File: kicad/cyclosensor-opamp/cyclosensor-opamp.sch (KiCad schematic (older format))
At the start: 11 parts, among them J1 RJ14, U1 LM358, U2 TCRT5000

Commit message: various changes to schematics
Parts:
- removed RV1, RV2: POT, ~, symbol POT
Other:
- moved on the sheet: GAIN1, J1, OFFSET1, R1, R2, R3, R5, U1A, U2

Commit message: updating basic cyclo-sensor.  Still need to verify with actual cyclophone.
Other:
- note added: "1M ok for tuning, not too sensitive?"
- note added: "Ok to have 5V without 'pair' here?"
- note added: "offset from which side? zero or 5v/1024?"
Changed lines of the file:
@@
 Sheet 1 1
 Title ""
-Date "5 apr 2014"
+Date "6 apr 2014"
 Rev ""
 Comp ""
@@
 Wire Wire Line
 	6800 3800 6800 3500
+Text Notes 6200 4200 0    60   ~ 0
+Ok to have 5V without 'pair' here?
+Text Notes 3200 5550 0    60   ~ 0
+offset from which side?  zero or 5v/1024?
+Text Notes 4100 3150 0    60   ~ 0
+1M ok for tuning, not too sensitive?
 $EndSCHEMATC

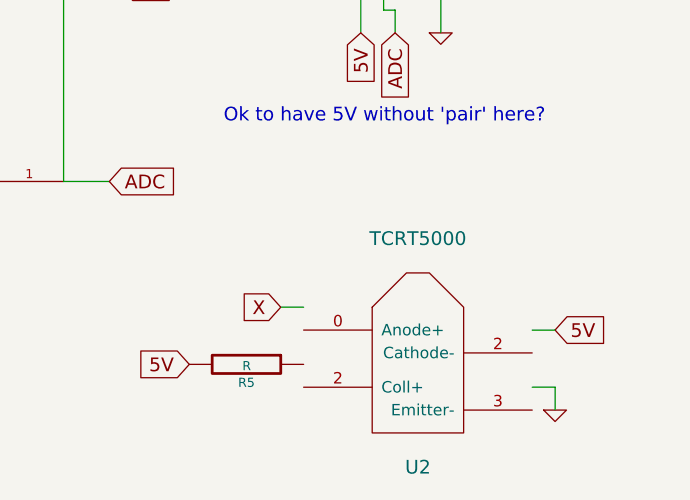
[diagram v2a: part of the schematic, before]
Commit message: add two voltage regulation circuits, the TL431 and LM317 based.  Also update some things - REFP is 2.5v, while AREF is 5v
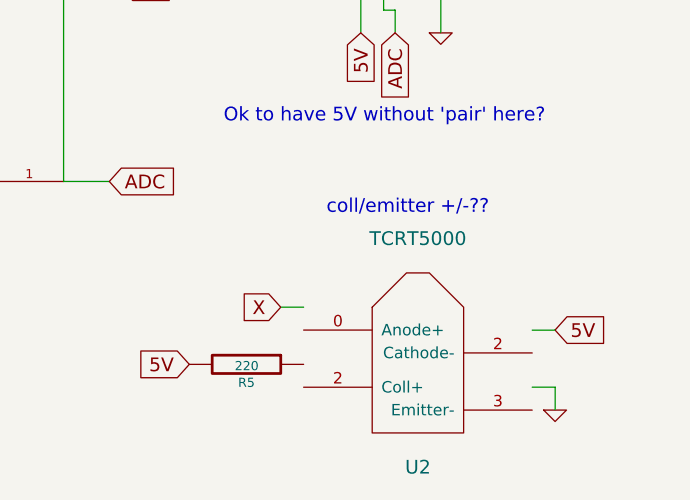
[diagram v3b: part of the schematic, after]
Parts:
- R5: value R -> 220
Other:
- note added: "coll/emitter +/-??"
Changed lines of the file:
@@
 P 6300 5250
 F 0 "R5" V 6380 5250 40  0000 C CNN
-F 1 "R" V 6307 5251 40  0000 C CNN
+F 1 "220" V 6307 5251 40  0000 C CNN
 F 2 "~" V 6230 5250 30  0000 C CNN
 F 3 "~" H 6300 5250 30  0000 C CNN
@@
 Text Notes 4100 3150 0    60   ~ 0
 1M ok for tuning, not too sensitive?
+Text Notes 6650 4600 0    60   ~ 0
+coll/emitter +/-??
 $EndSCHEMATC

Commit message: various changes!  notes frm Dan.
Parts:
- added C?: .01uf, ~, symbol C
- added C?: 10uf, ~, symbol C
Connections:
- wire segments 29 -> 33
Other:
- note added: "Ok to have 5V without 'pair' here? \nYES"
- note added: "Put near pin 8 on op-amp!"
- note added: "option of two caps \nfor different freq\nfiltering on each"
- note removed: "Ok to have 5V without 'pair' here?"
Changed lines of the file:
@@
 Sheet 1 1
 Title ""
-Date "6 apr 2014"
+Date "9 apr 2014"
 Rev ""
 Comp ""
@@
 	6800 3800 6800 3500
 Text Notes 6200 4200 0    60   ~ 0
-Ok to have 5V without 'pair' here?
+Ok to have 5V without 'pair' here?  \nYES
 Text Notes 3200 5550 0    60   ~ 0
 offset from which side?  zero or 5v/1024?
 Text Notes 4100 3150 0    60   ~ 0
 1M ok for tuning, not too sensitive?
-Text Notes 6650 4600 0    60   ~ 0
+Text Notes 6600 5950 0    60   ~ 0
 coll/emitter +/-??
+$Comp
+L C C?
+U 1 1 53449FBF
+P 8050 3800
+F 0 "C?" H 8050 3900 40  0000 L CNN
+F 1 ".01uf" H 8056 3715 40  0000 L CNN
+F 2 "~" H 8088 3650 30  0000 C CNN
+F 3 "~" H 8050 3800 60  0000 C CNN
+	1    8050 3800
+	1    0    0    -1
+$EndComp
+Text GLabel 8050 3450 1    60   Input ~ 0
+5V
+$Comp
+L GND #PWR?
+U 1 1 53449FDD
+P 8050 4100
+F 0 "#PWR?" H 8050 4100 30  0001 C CNN
+F 1 "GND" H 8050 4030 30  0001 C CNN
+F 2 "" H 8050 4100 60  0000 C CNN
+F 3 "" H 8050 4100 60  0000 C CNN
+	1    8050 4100
+	1    0    0    -1
+$EndComp
+Wire Wire Line
+	8050 4000 8050 4100
+Wire Wire Line
+	8050 3450 8050 3600
+Text Notes 7800 3200 0    60   ~ 0
+Put near pin 8 on op-amp!
+$Comp
+L C C?
+U 1 1 5344A0AE
+P 8400 3800
+F 0 "C?" H 8400 3900 40  0000 L CNN
+F 1 "10uf" H 8406 3715 40  0000 L CNN
+F 2 "~" H 8438 3650 30  0000 C CNN
+F 3 "~" H 8400 3800 60  0000 C CNN
+	1    8400 3800
+	1    0    0    -1
+$EndComp
+Text GLabel 8400 3450 1    60   Input ~ 0
+5V
+$Comp
+L GND #PWR?
+U 1 1 5344A0B5
+P 8400 4100
+F 0 "#PWR?" H 8400 4100 30  0001 C CNN
+F 1 "GND" H 8400 4030 30  0001 C CNN
+F 2 "" H 8400 4100 60  0000 C CNN
+F 3 "" H 8400 4100 60  0000 C CNN
+	1    8400 4100
+	1    0    0    -1
+$EndComp
+Wire Wire Line
+	8400 4000 8400 4100
+Wire Wire Line
+	8400 3450 8400 3600
+Text Notes 8050 4350 0    60   ~ 0
+option of two caps \nfor different freq\nfiltering on each
 $EndSCHEMATC

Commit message: update tcrt5000
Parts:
- removed R3: 1K, ~, symbol R
- removed U2: TCRT5000, ~, symbol TCRT5000
- added OFFSET?: 20K, ~, symbol POT
- added R?: 20k, ~, symbol R
- added U?: TCRT5000, ~, symbol TCRT5000
- GAIN1: value 1M -> 100k
- R1, R2: value 1K -> 20k
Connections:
- wire segments 33 -> 36
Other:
- moved on the sheet: OFFSET1, R5
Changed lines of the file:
@@
 Sheet 1 1
 Title ""
-Date "9 apr 2014"
+Date "12 apr 2014"
 Rev ""
 Comp ""
@@
 	1    0    0    -1
 $EndComp
-$Comp
-L TCRT5000 U2
-U 1 1 532FB873
-P 7050 5150
-F 0 "U2" H 7050 4600 60  0000 C CNN
-F 1 "TCRT5000" H 7050 5600 60  0000 C CNN
-F 2 "~" H 7050 5150 60  0000 C CNN
-F 3 "~" H 7050 5150 60  0000 C CNN
-	1    7050 5150
-	1    0    0    -1
-$EndComp
 Text GLabel 6800 3800 3    60   Input ~ 0
 5V
@@
 	1    0    0    -1
 $EndComp
-Text GLabel 4900 3950 1    60   Input ~ 0
+Text GLabel 4900 4950 3    60   Input ~ 0
 5V
 $Comp
 L GND #PWR02
 U 1 1 533B8353
-P 4900 4950
-F 0 "#PWR02" H 4900 4950 30  0001 C CNN
-F 1 "GND" H 4900 4880 30  0001 C CNN
-F 2 "" H 4900 4950 60  0000 C CNN
-F 3 "" H 4900 4950 60  0000 C CNN
-	1    4900 4950
-	1    0    0    -1
+P 4900 3950
+F 0 "#PWR02" H 4900 3950 30  0001 C CNN
+F 1 "GND" H 4900 3880 30  0001 C CNN
+F 2 "" H 4900 3950 60  0000 C CNN
+F 3 "" H 4900 3950 60  0000 C CNN
+	1    4900 3950
+	-1   0    0    1
 $EndComp
 $Comp
@@
 F 3 "" H 5000 4450 60  0000 C CNN
 	1    5000 4450
-	1    0    0    -1
+	1    0    0    1
 $EndComp
 $Comp
@@
 P 4000 4350
 F 0 "R2" V 4080 4350 40  0000 C CNN
-F 1 "1K" V 4007 4351 40  0000 C CNN
+F 1 "20k" V 4007 4351 40  0000 C CNN
 F 2 "~" V 3930 4350 30  0000 C CNN
 F 3 "~" H 4000 4350 30  0000 C CNN
@@
 ADC
 $Comp
-L R R3
-U 1 1 533B9B66
-P 4400 4900
-F 0 "R3" V 4480 4900 40  0000 C CNN
-F 1 "1K" V 4407 4901 40  0000 C CNN
-F 2 "~" V 4330 4900 30  0000 C CNN
-F 3 "~" H 4400 4900 30  0000 C CNN
-	1    4400 4900
-	1    0    0    -1
-$EndComp
-$Comp
 L R R1
 U 1 1 533B9B87
 P 3650 4750
 F 0 "R1" V 3730 4750 40  0000 C CNN
-F 1 "1K" V 3657 4751 40  0000 C CNN
+F 1 "20k" V 3657 4751 40  0000 C CNN
 F 2 "~" V 3580 4750 30  0000 C CNN
 F 3 "~" H 3650 4750 30  0000 C CNN
@@
 	1    0    0    -1
 $EndComp
-Text GLabel 5750 3600 2    60   Input ~ 0
-5V
-Text GLabel 7650 5100 2    60   Input ~ 0
-5V
-$Comp
-L GND #PWR03
-U 1 1 533B9C11
-P 3650 5150
-F 0 "#PWR03" H 3650 5150 30  0001 C CNN
-F 1 "GND" H 3650 5080 30  0001 C CNN
-F 2 "" H 3650 5150 60  0000 C CNN
-F 3 "" H 3650 5150 60  0000 C CNN
-	1    3650 5150
-	1    0    0    -1
-$EndComp
-$Comp
-L GND #PWR04
-U 1 1 533B9C20
-P 4400 5300
-F 0 "#PWR04" H 4400 5300 30  0001 C CNN
-F 1 "GND" H 4400 5230 30  0001 C CNN
-F 2 "" H 4400 5300 60  0000 C CNN
-F 3 "" H 4400 5300 60  0000 C CNN
-	1    4400 5300
-	1    0    0    -1
-$EndComp
-Text GLabel 6450 5000 0    60   Input ~ 0
+Text GLabel 2750 3750 0    60   Input ~ 0
 X
 Text GLabel 3550 4350 0    60   Input ~ 0
 X
-Text GLabel 6050 5250 0    60   Input ~ 0
+Text GLabel 2350 3500 0    60   Input ~ 0
 5V
 $Comp
 L GND #PWR05
 U 1 1 533B9F2F
-P 7650 5450
-F 0 "#PWR05" H 7650 5450 30  0001 C CNN
-F 1 "GND" H 7650 5380 30  0001 C CNN
-F 2 "" H 7650 5450 60  0000 C CNN
-F 3 "" H 7650 5450 60  0000 C CNN
-	1    7650 5450
+P 3950 3950
+F 0 "#PWR05" H 3950 3950 30  0001 C CNN
+F 1 "GND" H 3950 3880 30  0001 C CNN
+F 2 "" H 3950 3950 60  0000 C CNN
+F 3 "" H 3950 3950 60  0000 C CNN
+	1    3950 3950
 	1    0    0    -1
 $EndComp
@@
 L R R5
 U 1 1 533B9FB6
-P 6300 5250
-F 0 "R5" V 6380 5250 40  0000 C CNN
-F 1 "220" V 6307 5251 40  0000 C CNN
-F 2 "~" V 6230 5250 30  0000 C CNN
-F 3 "~" H 6300 5250 30  0000 C CNN
-	1    6300 5250
+P 2600 3500
+F 0 "R5" V 2680 3500 40  0000 C CNN
+F 1 "220" V 2607 3501 40  0000 C CNN
+F 2 "~" V 2530 3500 30  0000 C CNN
+F 3 "~" H 2600 3500 30  0000 C CNN
+	1    2600 3500
 	0    1    1    0
 $EndComp
 NoConn ~ 6700 3500
 NoConn ~ 7200 3500
-Wire Wire Line
-	7000 3500 7000 3650
-Wire Wire Line
-	7000 3650 7150 3650
-Wire Wire Line
-	4500 3450 4500 4350
-Wire Wire Line
-	4500 4350 4250 4350
-Wire Wire Line
-	3550 4350 3750 4350
-Wire Wire Line
-	3650 4350 3650 4500
-Connection ~ 3650 4350
-Wire Wire Line
-	6450 5000 6550 5000
-Wire Wire Line
-	7650 5100 7550 5100
-Wire Wire Line
-	5500 4450 5700 4450
-Wire Wire Line
-	4050 4550 4500 4550
-Wire Wire Line
-	4400 4550 4400 4650
-Wire Wire Line
-	4400 5150 4400 5300
-Wire Wire Line
-	3650 5000 3650 5150
-Wire Wire Line
-	5500 4450 5500 3600
-Connection ~ 5500 3600
-Wire Wire Line
-	4900 3950 4900 4050
-Wire Wire Line
-	6900 3500 6900 3700
-Wire Wire Line
-	6900 3700 6950 3700
-Wire Wire Line
-	6950 3700 6950 3800
-Wire Wire Line
-	7550 5350 7650 5350
-Wire Wire Line
-	7650 5350 7650 5450
 $Comp
 L POT GAIN1
@@
 P 4900 3450
 F 0 "GAIN1" H 4900 3350 50  0000 C CNN
-F 1 "1M" H 4900 3450 50  0000 C CNN
+F 1 "100k" H 4900 3450 50  0000 C CNN
 F 2 "~" H 4900 3450 60  0000 C CNN
 F 3 "~" H 4900 3450 60  0000 C CNN
@@
 	1    0    0    -1
 $EndComp
-Wire Wire Line
-	4500 3450 4650 3450
-Wire Wire Line
-	4900 3300 5250 3300
-Wire Wire Line
-	5250 3300 5250 3600
-Connection ~ 5250 3600
 NoConn ~ 5150 3450
-Wire Wire Line
-	5250 3600 5750 3600
 $Comp
 L POT OFFSET1
 U 1 1 533BA12C
-P 4050 4900
-F 0 "OFFSET1" H 4050 4800 50  0000 C CNN
-F 1 "20K" H 4050 4900 50  0000 C CNN
-F 2 "~" H 4050 4900 60  0000 C CNN
-F 3 "~" H 4050 4900 60  0000 C CNN
-	1    4050 4900
+P 4200 4800
+F 0 "OFFSET1" H 4200 4700 50  0000 C CNN
+F 1 "20K" H 4200 4800 50  0000 C CNN
+F 2 "~" H 4200 4800 60  0000 C CNN
+F 3 "~" H 4200 4800 60  0000 C CNN
+	1    4200 4800
 	0    1    1    0
 $EndComp
-Wire Wire Line
-	4050 4550 4050 4650
-Connection ~ 4400 4550
-Text GLabel 4200 5200 3    60   Input ~ 0
-5V
-Wire Wire Line
-	4200 4900 4200 5200
-NoConn ~ 4050 5150
-Wire Wire Line
-	4900 4850 4900 4950
-Wire Wire Line
-	7150 3650 7150 3800
+Text GLabel 4050 4550 0    60   Input ~ 0
+5V
 NoConn ~ 7100 3500
-Wire Wire Line
-	6800 3800 6800 3500
 Text Notes 6200 4200 0    60   ~ 0
 Ok to have 5V without 'pair' here?  \nYES
@@
 	1    0    0    -1
 $EndComp
-Wire Wire Line
-	8050 4000 8050 4100
-Wire Wire Line
-	8050 3450 8050 3600
 Text Notes 7800 3200 0    60   ~ 0
 Put near pin 8 on op-amp!
@@
 	1    0    0    -1
 $EndComp
-Wire Wire Line
-	8400 4000 8400 4100
-Wire Wire Line
-	8400 3450 8400 3600
 Text Notes 8050 4350 0    60   ~ 0
 option of two caps \nfor different freq\nfiltering on each
+$Comp
+L TCRT5000 U?
+U 1 1 53499E1E
+P 3350 3550
+F 0 "U?" H 3350 3000 60  0000 C CNN
+F 1 "TCRT5000" H 3350 4000 60  0000 C CNN
+F 2 "~" H 3350 3550 60  0000 C CNN
+F 3 "~" H 3350 3550 60  0000 C CNN
+	1    3350 3550
+	1    0    0    -1
+$EndComp
+Wire Wire Line
+	7000 3500 7000 3650
+Wire Wire Line
+	7000 3650 7150 3650
+Wire Wire Line
+	4500 3450 4500 4350
+Wire Wire Line
+	4500 4350 4250 4350
+Wire Wire Line
+	3550 4350 3750 4350
+Wire Wire Line
+	3650 4350 3650 4500
+Connection ~ 3650 4350
+Wire Wire Line
+	2750 3750 2850 3750
+Wire Wire Line
+	5500 4450 5700 4450
+Wire Wire Line
+	3650 5000 3650 5150
+Wire Wire Line
+	4900 3950 4900 4050
+Wire Wire Line
+	6900 3500 6900 3700
+Wire Wire Line
+	6900 3700 6950 3700
+Wire Wire Line
+	6950 3700 6950 3800
+Wire Wire Line
+	3850 3850 3950 3850
+Wire Wire Line
+	3950 3600 3950 3950
+Wire Wire Line
+	4500 3450 4650 3450
+Wire Wire Line
+	4900 4850 4900 4950
+Wire Wire Line
+	7150 3650 7150 3800
+Wire Wire Line
+	6800 3800 6800 3500
+Wire Wire Line
+	8050 4000 8050 4100
+Wire Wire Line
+	8050 3450 8050 3600
+Wire Wire Line
+	8400 4000 8400 4100
+Wire Wire Line
+	8400 3450 8400 3600
+Wire Wire Line
+	4900 3300 5500 3300
+Wire Wire Line
+	5500 3300 5500 4450
+Wire Wire Line
+	3950 3600 3850 3600
+Connection ~ 3950 3850
+Text GLabel 3650 5150 3    60   Input ~ 0
+5V
+$Comp
+L R R?
+U 1 1 5349C83F
+P 2550 4850
+F 0 "R?" V 2630 4850 40  0000 C CNN
+F 1 "20k" V 2557 4851 40  0000 C CNN
+F 2 "~" V 2480 4850 30  0000 C CNN
+F 3 "~" H 2550 4850 30  0000 C CNN
+	1    2550 4850
+	1    0    0    -1
+$EndComp
+$Comp
+L GND #PWR?
+U 1 1 5349C845
+P 2550 5250
+F 0 "#PWR?" H 2550 5250 30  0001 C CNN
+F 1 "GND" H 2550 5180 30  0001 C CNN
+F 2 "" H 2550 5250 60  0000 C CNN
+F 3 "" H 2550 5250 60  0000 C CNN
+	1    2550 5250
+	1    0    0    -1
+$EndComp
+$Comp
+L POT OFFSET?
+U 1 1 5349C84B
+P 2200 4850
+F 0 "OFFSET?" H 2200 4750 50  0000 C CNN
+F 1 "20K" H 2200 4850 50  0000 C CNN
+F 2 "~" H 2200 4850 60  0000 C CNN
+F 3 "~" H 2200 4850 60  0000 C CNN
+	1    2200 4850
+	0    1    1    0
+$EndComp
+Text GLabel 2350 5150 3    60   Input ~ 0
+5V
+NoConn ~ 2200 5100
+Wire Wire Line
+	2200 4500 2650 4500
+Wire Wire Line
+	2550 4500 2550 4600
+Wire Wire Line
+	2550 5100 2550 5250
+Wire Wire Line
+	2200 4500 2200 4600
+Connection ~ 2550 4500
+Wire Wire Line
+	2350 4850 2350 5150
+$Comp
+L GND #PWR?
+U 1 1 5349C88D
+P 4200 5150
+F 0 "#PWR?" H 4200 5150 30  0001 C CNN
+F 1 "GND" H 4200 5080 30  0001 C CNN
+F 2 "" H 4200 5150 60  0000 C CNN
+F 3 "" H 4200 5150 60  0000 C CNN
+	1    4200 5150
+	1    0    0    -1
+$EndComp
+Wire Wire Line
+	4350 4800 4400 4800
+Wire Wire Line
+	4400 4800 4400 4550
+Wire Wire Line
+	4400 4550 4500 4550
+Wire Wire Line
+	4050 4550 4200 4550
+Wire Wire Line
+	4200 5150 4200 5050
 $EndSCHEMATC

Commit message: more changes to match current test circuit.
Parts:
- OFFSET1: value 20K -> 10k
- R1, R2: value 20k -> 15k
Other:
- note added: "not used - change\nback to save on pots?"
- note removed: "coll/emitter +/-??"
- moved on the sheet: C?
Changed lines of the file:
@@
 Sheet 1 1
 Title ""
-Date "12 apr 2014"
+Date "13 apr 2014"
 Rev ""
 Comp ""
@@
 P 4000 4350
 F 0 "R2" V 4080 4350 40  0000 C CNN
-F 1 "20k" V 4007 4351 40  0000 C CNN
+F 1 "15k" V 4007 4351 40  0000 C CNN
 F 2 "~" V 3930 4350 30  0000 C CNN
 F 3 "~" H 4000 4350 30  0000 C CNN
@@
 P 3650 4750
 F 0 "R1" V 3730 4750 40  0000 C CNN
-F 1 "20k" V 3657 4751 40  0000 C CNN
+F 1 "15k" V 3657 4751 40  0000 C CNN
 F 2 "~" V 3580 4750 30  0000 C CNN
 F 3 "~" H 3650 4750 30  0000 C CNN
@@
 P 4200 4800
 F 0 "OFFSET1" H 4200 4700 50  0000 C CNN
-F 1 "20K" H 4200 4800 50  0000 C CNN
+F 1 "10k" H 4200 4800 50  0000 C CNN
 F 2 "~" H 4200 4800 60  0000 C CNN
 F 3 "~" H 4200 4800 60  0000 C CNN
@@
 Text Notes 4100 3150 0    60   ~ 0
 1M ok for tuning, not too sensitive?
-Text Notes 6600 5950 0    60   ~ 0
-coll/emitter +/-??
 $Comp
 L C C?
 U 1 1 53449FBF
-P 8050 3800
-F 0 "C?" H 8050 3900 40  0000 L CNN
-F 1 ".01uf" H 8056 3715 40  0000 L CNN
-F 2 "~" H 8088 3650 30  0000 C CNN
-F 3 "~" H 8050 3800 60  0000 C CNN
-	1    8050 3800
-	1    0    0    -1
-$EndComp
-Text GLabel 8050 3450 1    60   Input ~ 0
+P 6450 5250
+F 0 "C?" H 6450 5350 40  0000 L CNN
+F 1 ".01uf" H 6456 5165 40  0000 L CNN
+F 2 "~" H 6488 5100 30  0000 C CNN
+F 3 "~" H 6450 5250 60  0000 C CNN
+	1    6450 5250
+	1    0    0    -1
+$EndComp
+Text GLabel 6450 4900 1    60   Input ~ 0
 5V
 $Comp
 L GND #PWR?
 U 1 1 53449FDD
-P 8050 4100
-F 0 "#PWR?" H 8050 4100 30  0001 C CNN
-F 1 "GND" H 8050 4030 30  0001 C CNN
-F 2 "" H 8050 4100 60  0000 C CNN
-F 3 "" H 8050 4100 60  0000 C CNN
-	1    8050 4100
-	1    0    0    -1
-$EndComp
-Text Notes 7800 3200 0    60   ~ 0
+P 6450 5550
+F 0 "#PWR?" H 6450 5550 30  0001 C CNN
+F 1 "GND" H 6450 5480 30  0001 C CNN
+F 2 "" H 6450 5550 60  0000 C CNN
+F 3 "" H 6450 5550 60  0000 C CNN
+	1    6450 5550
+	1    0    0    -1
+$EndComp
+Text Notes 6200 4650 0    60   ~ 0
 Put near pin 8 on op-amp!
 $Comp
 L C C?
 U 1 1 5344A0AE
-P 8400 3800
-F 0 "C?" H 8400 3900 40  0000 L CNN
-F 1 "10uf" H 8406 3715 40  0000 L CNN
-F 2 "~" H 8438 3650 30  0000 C CNN
-F 3 "~" H 8400 3800 60  0000 C CNN
-	1    8400 3800
-	1    0    0    -1
-$EndComp
-Text GLabel 8400 3450 1    60   Input ~ 0
+P 6800 5250
+F 0 "C?" H 6800 5350 40  0000 L CNN
+F 1 "10uf" H 6806 5165 40  0000 L CNN
+F 2 "~" H 6838 5100 30  0000 C CNN
+F 3 "~" H 6800 5250 60  0000 C CNN
+	1    6800 5250
+	1    0    0    -1
+$EndComp
+Text GLabel 6800 4900 1    60   Input ~ 0
 5V
 $Comp
 L GND #PWR?
 U 1 1 5344A0B5
-P 8400 4100
-F 0 "#PWR?" H 8400 4100 30  0001 C CNN
-F 1 "GND" H 8400 4030 30  0001 C CNN
-F 2 "" H 8400 4100 60  0000 C CNN
-F 3 "" H 8400 4100 60  0000 C CNN
-	1    8400 4100
-	1    0    0    -1
-$EndComp
-Text Notes 8050 4350 0    60   ~ 0
+P 6800 5550
+F 0 "#PWR?" H 6800 5550 30  0001 C CNN
+F 1 "GND" H 6800 5480 30  0001 C CNN
+F 2 "" H 6800 5550 60  0000 C CNN
+F 3 "" H 6800 5550 60  0000 C CNN
+	1    6800 5550
+	1    0    0    -1
+$EndComp
+Text Notes 6450 5800 0    60   ~ 0
 option of two caps \nfor different freq\nfiltering on each
 $Comp
@@
 	6800 3800 6800 3500
 Wire Wire Line
-	8050 4000 8050 4100
-Wire Wire Line
-	8050 3450 8050 3600
-Wire Wire Line
-	8400 4000 8400 4100
-Wire Wire Line
-	8400 3450 8400 3600
+	6450 5450 6450 5550
+Wire Wire Line
+	6450 4900 6450 5050
+Wire Wire Line
+	6800 5450 6800 5550
+Wire Wire Line
+	6800 4900 6800 5050
 Wire Wire Line
 	4900 3300 5500 3300
@@
 Wire Wire Line
 	4200 5150 4200 5050
+Text Notes 1850 4350 0    60   ~ 0
+not used - change\nback to save on pots?
 $EndSCHEMATC

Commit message: tweak a few things
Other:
- moved on the sheet: OFFSET1
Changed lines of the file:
@@
 Sheet 1 1
 Title ""
-Date "13 apr 2014"
+Date "16 apr 2014"
 Rev ""
 Comp ""
@@
 L POT OFFSET1
 U 1 1 533BA12C
-P 4200 4800
-F 0 "OFFSET1" H 4200 4700 50  0000 C CNN
-F 1 "10k" H 4200 4800 50  0000 C CNN
-F 2 "~" H 4200 4800 60  0000 C CNN
-F 3 "~" H 4200 4800 60  0000 C CNN
-	1    4200 4800
-	0    1    1    0
-$EndComp
-Text GLabel 4050 4550 0    60   Input ~ 0
+P 4400 5000
+F 0 "OFFSET1" H 4400 4900 50  0000 C CNN
+F 1 "10k" H 4400 5000 50  0000 C CNN
+F 2 "~" H 4400 5000 60  0000 C CNN
+F 3 "~" H 4400 5000 60  0000 C CNN
+	1    4400 5000
+	1    0    0    -1
+$EndComp
+Text GLabel 4150 5150 3    60   Input ~ 0
 5V
 NoConn ~ 7100 3500
@@
 L GND #PWR?
 U 1 1 5349C88D
-P 4200 5150
-F 0 "#PWR?" H 4200 5150 30  0001 C CNN
-F 1 "GND" H 4200 5080 30  0001 C CNN
-F 2 "" H 4200 5150 60  0000 C CNN
-F 3 "" H 4200 5150 60  0000 C CNN
-	1    4200 5150
-	1    0    0    -1
-$EndComp
-Wire Wire Line
-	4350 4800 4400 4800
-Wire Wire Line
-	4400 4800 4400 4550
+P 4650 5200
+F 0 "#PWR?" H 4650 5200 30  0001 C CNN
+F 1 "GND" H 4650 5130 30  0001 C CNN
+F 2 "" H 4650 5200 60  0000 C CNN
+F 3 "" H 4650 5200 60  0000 C CNN
+	1    4650 5200
+	1    0    0    -1
+$EndComp
+Wire Wire Line
+	4400 4550 4400 4850
 Wire Wire Line
 	4400 4550 4500 4550
 Wire Wire Line
-	4050 4550 4200 4550
-Wire Wire Line
-	4200 5150 4200 5050
+	4150 5150 4150 5000
 Text Notes 1850 4350 0    60   ~ 0
 not used - change\nback to save on pots?
+Wire Wire Line
+	4650 5000 4650 5200
 $EndSCHEMATC
